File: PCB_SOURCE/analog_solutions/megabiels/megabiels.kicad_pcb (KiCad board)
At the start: 2 copper layers, 150 x 30 mm, 8 parts, among them J101 Conn_01x01_Pin, J102 Conn_01x01_Pin

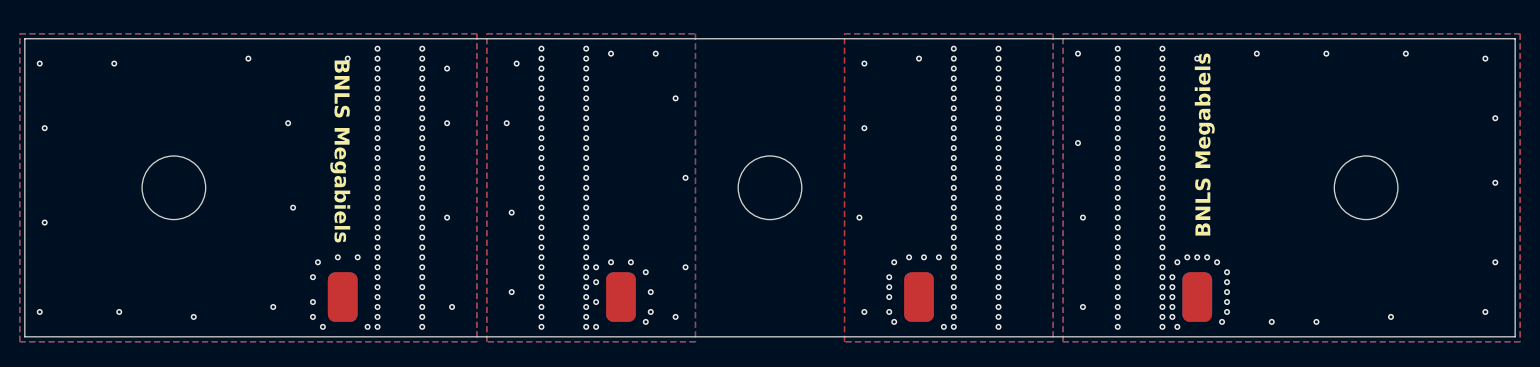
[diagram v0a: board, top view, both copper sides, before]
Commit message: fixed bug in ahob program among others
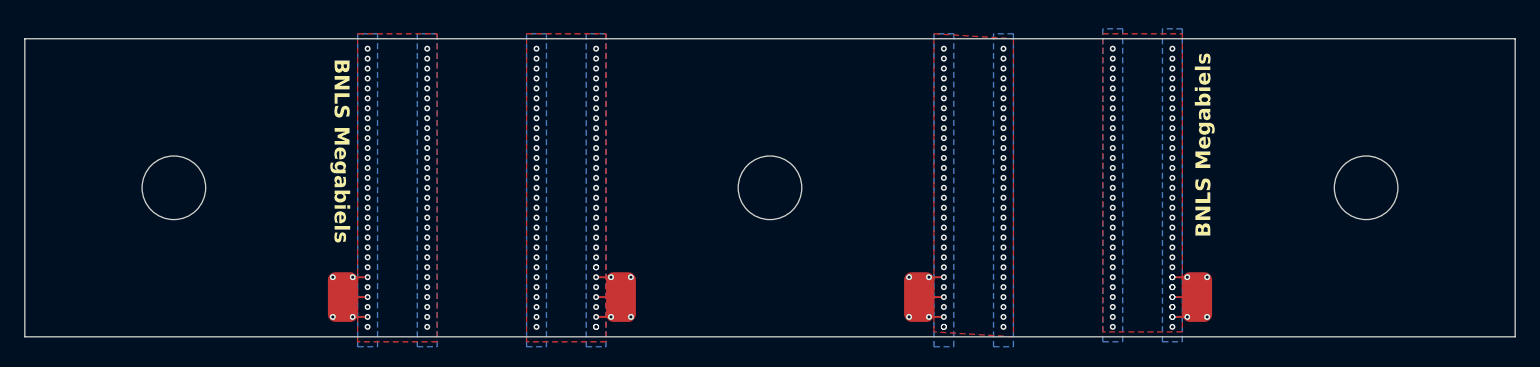
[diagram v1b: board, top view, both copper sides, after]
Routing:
- net /B: track 0.00 -> 12.5 mm, vias 155 -> 125
- net /A: track 0.00 -> 11.0 mm, vias 169 -> 131
